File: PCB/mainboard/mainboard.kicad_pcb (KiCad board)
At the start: 2 copper layers, 22 parts, among them J1 VBuck, J2 Temp, J3 Hall, J4 Display, U1 ATmega8-16A, Y1 16MHz

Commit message: Add files via upload
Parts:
- added C3: 100nF, Capacitor_SMD:C_0805_2012Metric, F.Cu at (135.8, 54.7)
- added D1: D, Diode_SMD:D_0805_2012Metric, F.Cu at (139.7, 52.8)
- added R10: 0, Resistor_SMD:R_0805_2012Metric, F.Cu at (114.5, 48.9)
- added R11: 0, Resistor_SMD:R_0805_2012Metric, F.Cu at (114.5, 52.2)
- added R12: 0, Resistor_SMD:R_0805_2012Metric, F.Cu at (114.5, 55.6)
- added R13: 0, Resistor_SMD:R_0805_2012Metric, F.Cu at (114.7, 58.8)
- added R7: 10k, Resistor_SMD:R_0805_2012Metric, F.Cu at (143.3, 51.3)
- added R8: 0, Resistor_SMD:R_0805_2012Metric, F.Cu at (119.5, 48.1)
- added R9: 0, Resistor_SMD:R_0805_2012Metric, F.Cu at (114.7, 40.8)
- added SW1: SW_Push, Button_Switch_THT:SW_PUSH_6mm, F.Cu at (149.4, 40.7)
- moved H2 27.7 mm to (150.0, 62.2)
- moved C2 20.7 mm to (122.9, 37.3), turned to -90 degrees
- moved J3 19.6 mm to (141.5, 34.5)
- moved C1 18.5 mm to (127.3, 37.3), turned to -90 degrees
- moved C6 17.9 mm to (149.7, 53.3), turned to 0 degrees
- moved R3 14.5 mm to (121.7, 59.7)
- moved J2 14.4 mm to (151.6, 34.2)
- moved Y1 13.6 mm to (124.7, 41.4), turned to 0 degrees
- moved R1 13.6 mm to (131.8, 59.4), turned to 90 degrees
- moved C5 12.6 mm to (141.6, 63.2), turned to -90 degrees
- moved R2 12.3 mm to (128.3, 59.6), turned to 180 degrees
- moved RV1 12.2 mm to (124.6, 32.9)
- moved C4 12.1 mm to (125.2, 59.8), turned to -90 degrees
- moved H1 10.6 mm to (118.1, 28.4)
- moved R4 9.82 mm to (135.5, 51.1), turned to 180 degrees
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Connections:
- C1 pad 1: Vss -> GND
- C2 pad 1: Vss -> GND
- C4 pad 2: Vss -> GND
- C5 pad 2: Vss -> GND
- C6 pad 2: Vss -> GND
- C7 pad 2: Vss -> GND
- C8 pad 2: Vss -> GND
- H1 pad 1: Vss -> GND
- H2 pad 1: Vss -> GND
- J1 pad 1: Vss -> GND
- J2 pad 2: Vss -> GND
- J3 pad 2: Vss -> GND
- J4 pad 11: unconnected-(J4-Pad11) -> Net-(J4-Pad11)
- J4 pad 12: unconnected-(J4-Pad12) -> Net-(J4-Pad12)
- J4 pad 13: unconnected-(J4-Pad13) -> Net-(J4-Pad13)
- J4 pad 14: unconnected-(J4-Pad14) -> Net-(J4-Pad14)
- J4 pad 16: Vss -> GND
- J4 pad 2: VCC -> Vdd
- J4 pad 4: unconnected-(J4-Pad4) -> Net-(J4-Pad4)
- J4 pad 5: Vss -> GND
- J4 pad 6: unconnected-(J4-Pad6) -> Net-(J4-Pad6)
- R2 pad 2: Vss -> GND
- RV1 pad 1: Vss -> GND
- U1 pad 12: unconnected-(U1-Pad12) -> /PB0
- U1 pad 13: unconnected-(U1-Pad13) -> /PB1
- U1 pad 14: unconnected-(U1-Pad14) -> /PB2
- U1 pad 15: unconnected-(U1-Pad15) -> /PB3
- U1 pad 16: unconnected-(U1-Pad16) -> /PB4
- U1 pad 17: unconnected-(U1-Pad17) -> /PB5
- U1 pad 21: Vss -> GND
- U1 pad 29: unconnected-(U1-Pad29) -> RESET
- U1 pad 3: Vss -> GND
- U1 pad 5: Vss -> GND
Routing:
- net Vss: track 108.3 -> 0.00 mm, vias 4 -> 0
- net RESET: track 0.00 -> 30.0 mm, vias 0 -> 1
- net VCC: track 105.8 -> 125.4 mm, vias 4 -> 2
- net Temp: track 12.1 -> 30.6 mm
- net Net-(J4-Pad4): track 0.00 -> 18.1 mm
- net /PB1: track 0.00 -> 15.6 mm
- net GND: track 0.00 -> 10.9 mm, vias 0 -> 11
- net /PB5: track 0.00 -> 9.84 mm
- net /PB2: track 0.00 -> 9.43 mm
- net /PB3: track 0.00 -> 8.39 mm
- net /PB4: track 0.00 -> 7.82 mm
- net /PB0: track 0.00 -> 5.07 mm
- net Net-(J4-Pad6): track 0.00 -> 4.37 mm
- net Net-(J4-Pad11): track 0.00 -> 4.21 mm
- net Net-(J4-Pad12): track 0.00 -> 3.90 mm
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- added copper zone on B.Cu, net GND
- added copper zone on F.Cu, net GND
- removed copper zone on B.Cu, net (none)
- removed copper zone on F.Cu, net (none)
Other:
- board outline added: 45.2 x 43.6 mm

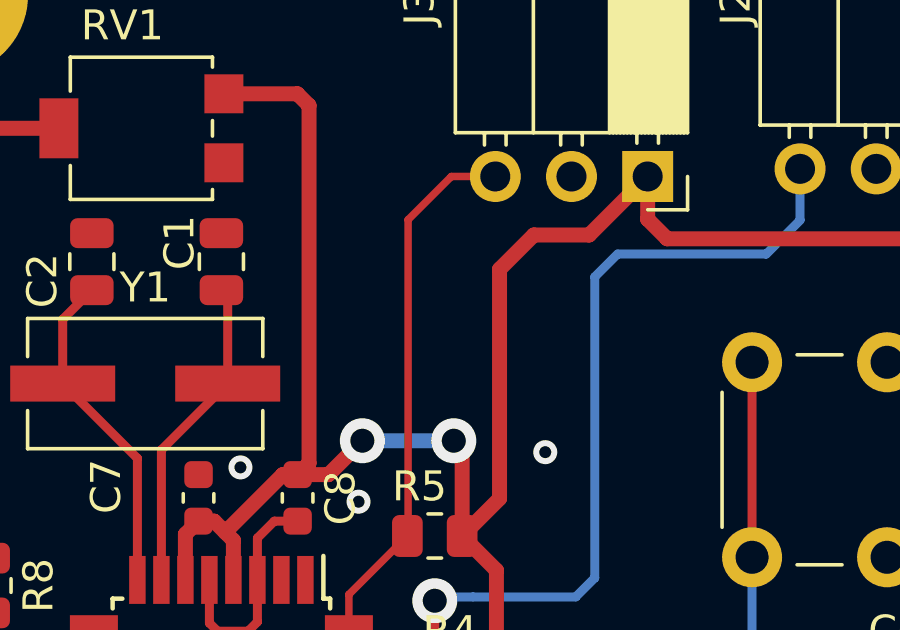
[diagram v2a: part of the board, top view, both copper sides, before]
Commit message: PCB error correction
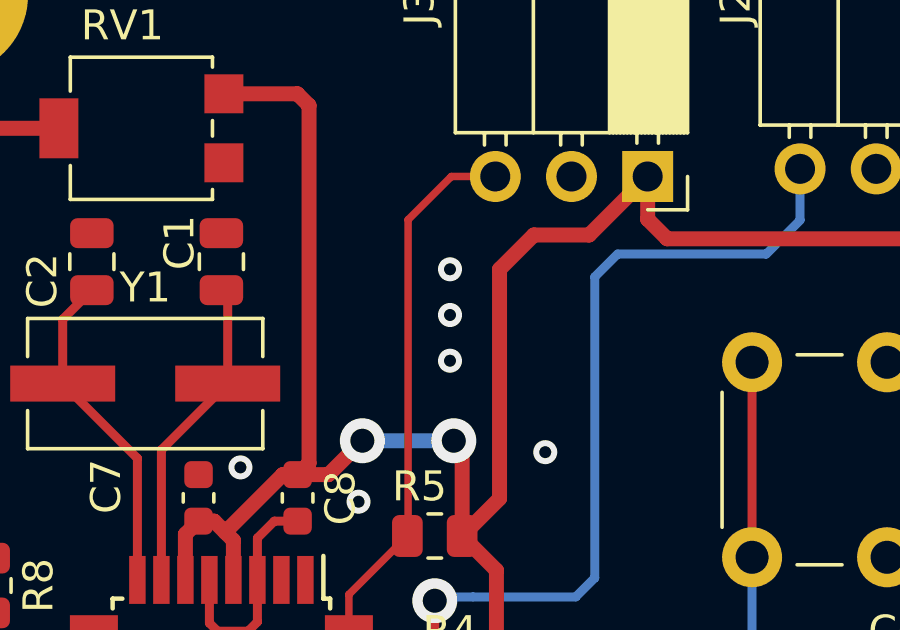
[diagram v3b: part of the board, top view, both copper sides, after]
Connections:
- J4 pad 1: Vss -> GND
- J4 pad 2: Vdd -> VCC
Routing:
- net GND: vias 11 -> 14

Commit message: Add files via upload
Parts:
- moved H1 8.26 mm to (126.4, 28.2)
- moved RV1 5.18 mm to (119.6, 31.4), turned to 0 degrees
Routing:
- net VCC: track 125.4 -> 142.8 mm
- net V0: track 11.8 -> 10.1 mm
- net GND: vias 14 -> 19
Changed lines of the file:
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@@
       (drillshape 0)
       (scaleselection 1)
-      (outputdirectory "./gerber")
+      (outputdirectory "gerber1/")
     )
   )
@@
   )
   (footprint "MountingHole:MountingHole_2.7mm_M2.5_Pad" (layer "F.Cu")
-    (at 118.11 28.448)
+    (at 126.365 28.194)
     (descr "Mounting Hole 2.7mm, M2.5")
     (tags "mounting hole 2.7mm m2.5")
@@
     (property "Sheetname" "")
     (attr exclude_from_pos_files)
-    (fp_text reference "H1" (at 0 -3.7) (layer "F.SilkS")
+    (fp_text reference "H1" (at -2.667 -2.667) (layer "F.SilkS")
       (effects (font (size 1 1) (thickness 0.15)))
     )
@@
   )
   (footprint "Potentiometer_SMD:Potentiometer_Bourns_3314G_Vertical" (layer "F.Cu")
-    (at 124.587 32.893 -90)
+    (at 119.634 31.369)
     (descr "Potentiometer, vertical, Bourns 3314G, http://www.bourns.com/docs/Product-Datasheets/3314.pdf")
     (tags "Potentiometer vertical Bourns 3314G")
@@
     (property "Sheetname" "")
     (attr smd)
-    (fp_text reference "RV1" (at -3.429 0.635 180) (layer "F.SilkS")
-      (effects (font (size 1 1) (thickness 0.15)))
-    )
-    (fp_text value "Poti" (at 0 4.65 90) (layer "F.Fab")
-      (effects (font (size 1 1) (thickness 0.15)))
-    )
-    (fp_text user "${REFERENCE}" (at 0 -1.7 90) (layer "F.Fab")
+    (fp_text reference "RV1" (at -3.429 0.635 90) (layer "F.SilkS")
+      (effects (font (size 1 1) (thickness 0.15)))
+    )
+    (fp_text value "Poti" (at 0 4.65) (layer "F.Fab")
+      (effects (font (size 1 1) (thickness 0.15)))
+    )
+    (fp_text user "${REFERENCE}" (at 0 -1.7) (layer "F.Fab")
       (effects (font (size 0.63 0.63) (thickness 0.15)))
     )
@@
     (fp_line (start 0 0.99) (end 0.001 -0.989) (layer "F.Fab") (width 0.1))
     (fp_circle (center 0 0) (end 1 0) (layer "F.Fab") (width 0.1) (fill none))
-    (pad "1" smd rect (at 1.15 -2.75 270) (size 1.3 1.3) (layers "F.Cu" "F.Paste" "F.Mask")
+    (pad "1" smd rect (at 1.15 -2.75) (size 1.3 1.3) (layers "F.Cu" "F.Paste" "F.Mask")
       (net 8 "GND") (pinfunction "1") (pintype "passive"))
-    (pad "2" smd rect (at 0 2.75 270) (size 2 1.3) (layers "F.Cu" "F.Paste" "F.Mask")
+    (pad "2" smd rect (at 0 2.75) (size 2 1.3) (layers "F.Cu" "F.Paste" "F.Mask")
       (net 7 "V0") (pinfunction "2") (pintype "passive"))
-    (pad "3" smd rect (at -1.15 -2.75 270) (size 1.3 1.3) (layers "F.Cu" "F.Paste" "F.Mask")
+    (pad "3" smd rect (at -1.15 -2.75) (size 1.3 1.3) (layers "F.Cu" "F.Paste" "F.Mask")
       (net 4 "VCC") (pinfunction "3") (pintype "passive"))
     (model "${KICAD6_3DMODEL_DIR}/Potentiometer_SMD.3dshapes/Potentiometer_Bourns_3314G_Vertical.wrl"
@@
   (segment (start 136.4215 51.054) (end 138.8595 51.054) (width 0.5) (layer "F.Cu") (net 4))
   (segment (start 143.256 50.3955) (end 141.199 50.3955) (width 0.5) (layer "F.Cu") (net 4))
-  (segment (start 130.175 44.056) (end 129.794 44.437) (width 0.5) (layer "F.Cu") (net 4))
-  (segment (start 130.175 32.131) (end 130.175 44.056) (width 0.5) (layer "F.Cu") (net 4))
   (segment (start 142.113 36.576) (end 141.463 35.926) (width 0.5) (layer "F.Cu") (net 4))
   (segment (start 127.654 47.947) (end 127.654 46.628) (width 0.5) (layer "F.Cu") (net 4))
@@
   (segment (start 137.668 36.449) (end 139.513 36.449) (width 0.5) (layer "F.Cu") (net 4))
   (segment (start 130.823 44.437) (end 129.794 44.437) (width 0.5) (layer "F.Cu") (net 4))
+  (segment (start 118.484 28.619) (end 118.484 29.838) (width 0.5) (layer "F.Cu") (net 4))
   (segment (start 136.4215 47.625) (end 136.4215 51.054) (width 0.5) (layer "F.Cu") (net 4))
   (segment (start 116.987 64.745) (end 121.1295 60.6025) (width 0.5) (layer "F.Cu") (net 4))
   (segment (start 131.953 62.484) (end 140.167 62.484) (width 0.5) (layer "F.Cu") (net 4))
+  (segment (start 128.143 32.131) (end 129.794 33.782) (width 0.5) (layer "F.Cu") (net 4))
   (segment (start 129.794 44.437) (end 129.299 44.437) (width 0.5) (layer "F.Cu") (net 4))
   (segment (start 115.4665 63.2245) (end 116.987 64.745) (width 0.5) (layer "F.Cu") (net 4))
@@
   (segment (start 127.654 46.628) (end 127.381 46.355) (width 0.5) (layer "F.Cu") (net 4))
   (segment (start 151.623 34.245) (end 151.623 35.702) (width 0.5) (layer "F.Cu") (net 4))
+  (segment (start 118.147 28.956) (end 118.484 28.619) (width 0.5) (layer "F.Cu") (net 4))
   (segment (start 121.666 60.96) (end 123.19 62.484) (width 0.5) (layer "F.Cu") (net 4))
   (segment (start 121.666 60.6025) (end 121.666 60.96) (width 0.5) (layer "F.Cu") (net 4))
-  (segment (start 127.337 31.743) (end 129.787 31.743) (width 0.5) (layer "F.Cu") (net 4))
   (segment (start 145.2645 50.3955) (end 143.256 50.3955) (width 0.5) (layer "F.Cu") (net 4))
   (segment (start 138.8595 51.054) (end 139.7 51.8945) (width 0.5) (layer "F.Cu") (net 4))
   (segment (start 140.167 62.484) (end 141.605 61.046) (width 0.5) (layer "F.Cu") (net 4))
+  (segment (start 120.777 32.131) (end 128.143 32.131) (width 0.5) (layer "F.Cu") (net 4))
+  (segment (start 118.484 29.838) (end 120.777 32.131) (width 0.5) (layer "F.Cu") (net 4))
   (segment (start 127.013 45.987) (end 126.492 45.987) (width 0.5) (layer "F.Cu") (net 4))
   (segment (start 126.054 47.947) (end 126.054 46.425) (width 0.5) (layer "F.Cu") (net 4))
   (segment (start 147.533 57.191) (end 147.533 53.34) (width 0.5) (layer "F.Cu") (net 4))
   (segment (start 131.826 62.357) (end 131.953 62.484) (width 0.5) (layer "F.Cu") (net 4))
+  (segment (start 110.617 28.956) (end 118.147 28.956) (width 0.5) (layer "F.Cu") (net 4))
   (segment (start 115.4665 61.976) (end 115.4665 63.2245) (width 0.5) (layer "F.Cu") (net 4))
   (segment (start 150.749 36.576) (end 142.113 36.576) (width 0.5) (layer "F.Cu") (net 4))
-  (segment (start 129.787 31.743) (end 130.175 32.131) (width 0.5) (layer "F.Cu") (net 4))
+  (segment (start 129.794 33.782) (end 129.794 44.437) (width 0.5) (layer "F.Cu") (net 4))
   (segment (start 127.381 46.355) (end 127.013 45.987) (width 0.5) (layer "F.Cu") (net 4))
   (segment (start 147.533 52.664) (end 145.2645 50.3955) (width 0.5) (layer "F.Cu") (net 4))
@@
   (segment (start 131.504 49.397) (end 131.504 48.4315) (width 0.25) (layer "F.Cu") (net 6))
   (segment (start 131.504 48.4315) (end 133.4535 46.482) (width 0.25) (layer "F.Cu") (net 6))
-  (segment (start 112.014 32.893) (end 110.617 31.496) (width 0.5) (layer "F.Cu") (net 7))
-  (segment (start 121.837 32.893) (end 112.014 32.893) (width 0.5) (layer "F.Cu") (net 7))
+  (segment (start 117.011 31.496) (end 119.634 34.119) (width 0.5) (layer "F.Cu") (net 7))
+  (segment (start 110.617 31.496) (end 117.011 31.496) (width 0.5) (layer "F.Cu") (net 7))
   (segment (start 128.454 47.947) (end 128.454 46.552) (width 0.3) (layer "F.Cu") (net 8))
   (segment (start 128.454 49.346) (end 128.454 47.947) (width 0.3) (layer "F.Cu") (net 8))
@@
   (via (at 138.049 43.688) (size 0.8) (drill 0.4) (layers "F.Cu" "B.Cu") (free) (net 8))
   (via (at 134.874 40.64) (size 0.8) (drill 0.4) (layers "F.Cu" "B.Cu") (free) (net 8))
+  (via (at 115.951 33.655) (size 0.8) (drill 0.4) (layers "F.Cu" "B.Cu") (free) (net 8))
   (via (at 114.681 53.848) (size 0.8) (drill 0.4) (layers "F.Cu" "B.Cu") (free) (net 8))
   (via (at 134.874 37.592) (size 0.8) (drill 0.4) (layers "F.Cu" "B.Cu") (free) (net 8))
   (via (at 117.602 52.578) (size 0.8) (drill 0.4) (layers "F.Cu" "B.Cu") (free) (net 8))
+  (via (at 117.729 35.687) (size 0.8) (drill 0.4) (layers "F.Cu" "B.Cu") (free) (net 8))
+  (via (at 115.206982 30.232305) (size 0.8) (drill 0.4) (layers "F.Cu" "B.Cu") (free) (net 8))
   (via (at 126.619 61.087) (size 0.8) (drill 0.4) (layers "F.Cu" "B.Cu") (free) (net 8))
   (via (at 113.665 44.196) (size 0.8) (drill 0.4) (layers "F.Cu" "B.Cu") (free) (net 8))
   (via (at 137.541 52.578) (size 0.8) (drill 0.4) (layers "F.Cu" "B.Cu") (free) (net 8))
+  (via (at 116.84 34.671) (size 0.8) (drill 0.4) (layers "F.Cu" "B.Cu") (free) (net 8))
   (via (at 117.348 56.515) (size 0.8) (drill 0.4) (layers "F.Cu" "B.Cu") (free) (net 8))
   (via (at 127.889 44.196) (size 0.8) (drill 0.4) (layers "F.Cu" "B.Cu") (free) (net 8))
   (via (at 134.874 39.116) (size 0.8) (drill 0.4) (layers "F.Cu" "B.Cu") (free) (net 8))
+  (via (at 113.665 30.226) (size 0.8) (drill 0.4) (layers "F.Cu" "B.Cu") (free) (net 8))
   (via (at 119.253 59.436) (size 0.8) (drill 0.4) (layers "F.Cu" "B.Cu") (free) (net 8))
   (via (at 140.081 58.293) (size 0.8) (drill 0.4) (layers "F.Cu" "B.Cu") (free) (net 8))

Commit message: Add files via upload
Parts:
- moved D1 3.49 mm to (141.6, 49.9), turned to 90 degrees
- moved C3 2.08 mm to (134.1, 56.0)
- moved R7 1.89 mm to (144.5, 49.9), turned to 90 degrees
- moved SW1 1.62 mm to (150.6, 39.5)
- moved H2 1.02 mm to (150.0, 63.2)
- moved R2 1.00 mm to (129.3, 59.4), turned to -90 degrees
- moved C2 0.99 mm to (122.0, 37.1)
- moved R4 0.89 mm to (136.4, 51.0)
- moved R1 0.64 mm to (132.5, 59.4)
- moved J3 0.25 mm to (141.5, 34.2)
- moved C1 0.21 mm to (127.5, 37.3)
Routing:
- net VCC: track 142.8 -> 78.2 mm
- net RESET: track 30.0 -> 21.4 mm
- net Temp: track 30.6 -> 25.6 mm
- net GND: track 10.9 -> 14.5 mm, vias 19 -> 27
- net ADC6: track 6.22 -> 5.28 mm
- net Hall1: track 17.8 -> 17.2 mm
- added copper zone on F.Cu, net RESET
- added copper zone on F.Cu, net VCC

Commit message: Release v1.0
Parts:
- J1: footprint Connector_PinSocket_2.54mm:PinSocket_1x02_P2.54mm_Vertical -> Connector_PinSocket_2.54mm:PinSocket_1x03_P2.54mm_Vertical
- moved R2 53.7 mm to (143.9, 111.1)
- moved R1 52.9 mm to (147.1, 110.2), turned to 180 degrees
- moved C3 52.4 mm to (143.6, 107.6), turned to 0 degrees
- moved C5 52.2 mm to (153.5, 114.0)
- moved H2 51.9 mm to (160.8, 114.0)
- moved J2 51.9 mm to (162.4, 85.0)
- moved J3 51.9 mm to (152.3, 85.0)
- moved R4 51.9 mm to (147.2, 101.8)
- moved D1 51.9 mm to (152.4, 100.7)
- moved R3 51.9 mm to (132.5, 110.5)
- moved C1 51.9 mm to (138.3, 88.1)
- moved C4 51.9 mm to (136.0, 110.6)
- moved R12 51.9 mm to (125.3, 106.4)
- moved R8 51.9 mm to (130.3, 98.9)
- moved SW1 51.9 mm to (161.4, 90.3)
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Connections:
- J1 pad 2: VCC -> ADC6
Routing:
- net ADC6: track 5.28 -> 23.5 mm, vias 0 -> 1
- net RESET: track 21.4 -> 21.9 mm
